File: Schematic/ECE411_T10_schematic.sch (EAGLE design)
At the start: 64 parts, among them IC1 LM386MM-1, J1 1, J2 DCJ0202, J3 AVR_SPI_PRG_6PTH, Q1 8.192 MHz, SW1 SPST_TACT-EVQQ2, U1 ATMEGA328P_PDIP

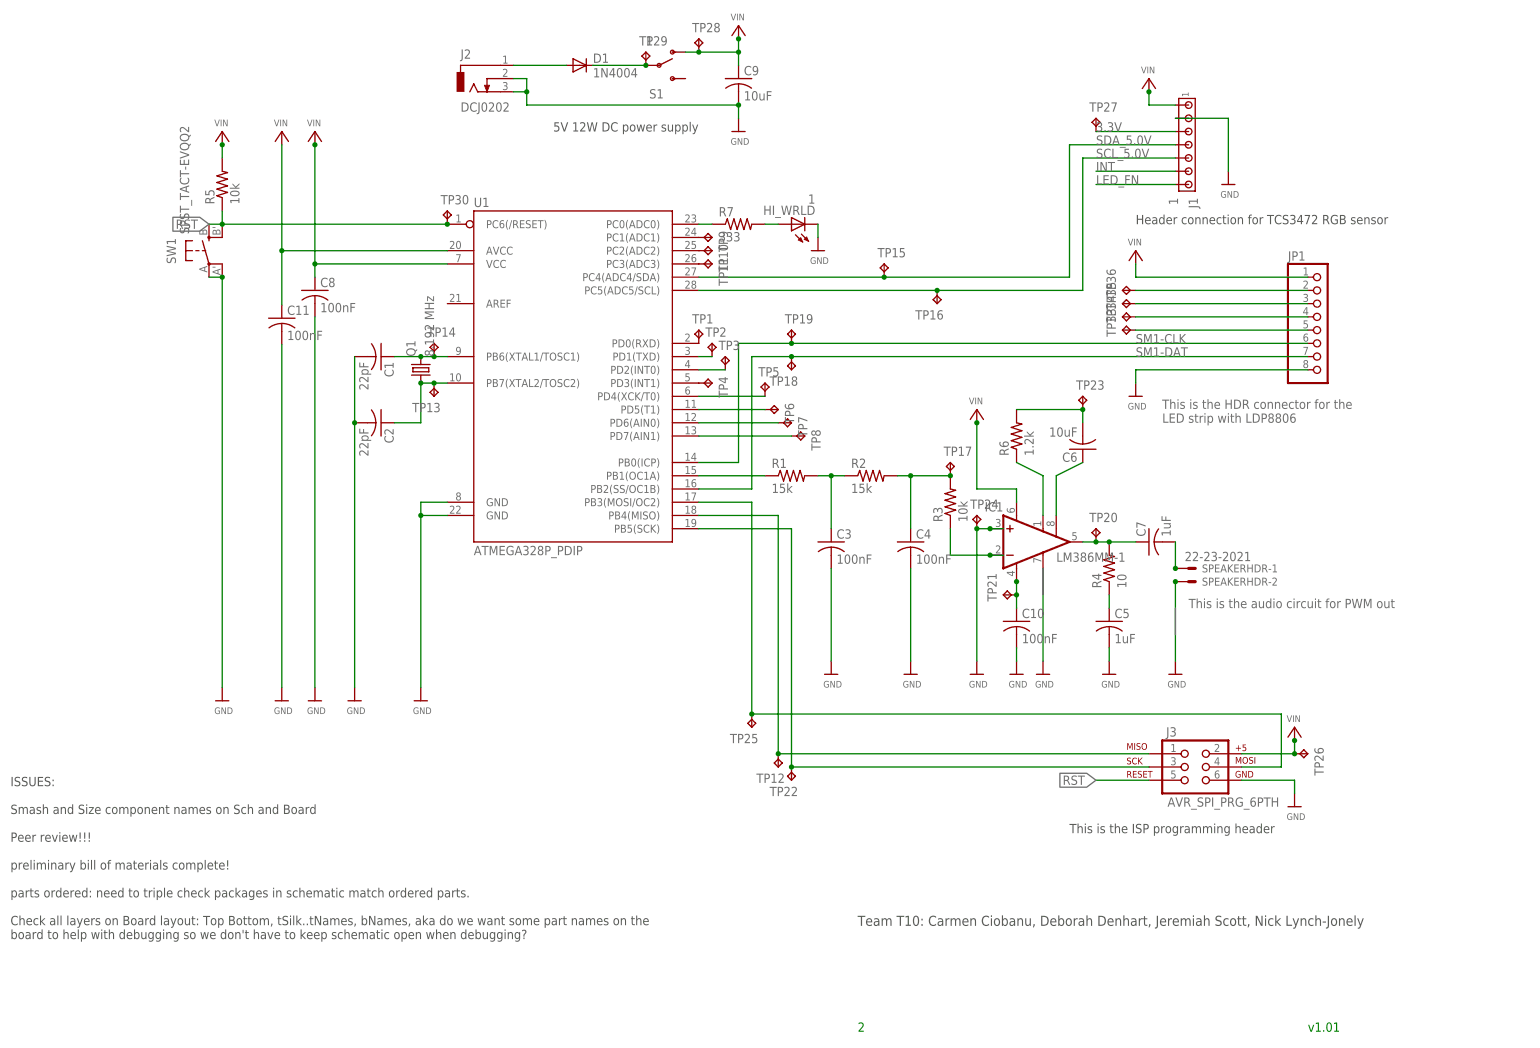
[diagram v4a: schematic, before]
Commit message: final layout candidate?
- fixed airwire @ (1.30, 1.05)
- smashed/sized some test points on Schematic
- updated dimension layer of board layout for better spacing of mounting
holes
- added team name info to both tPlace and tSilk layers
- png screenshots of final board layout candidate?
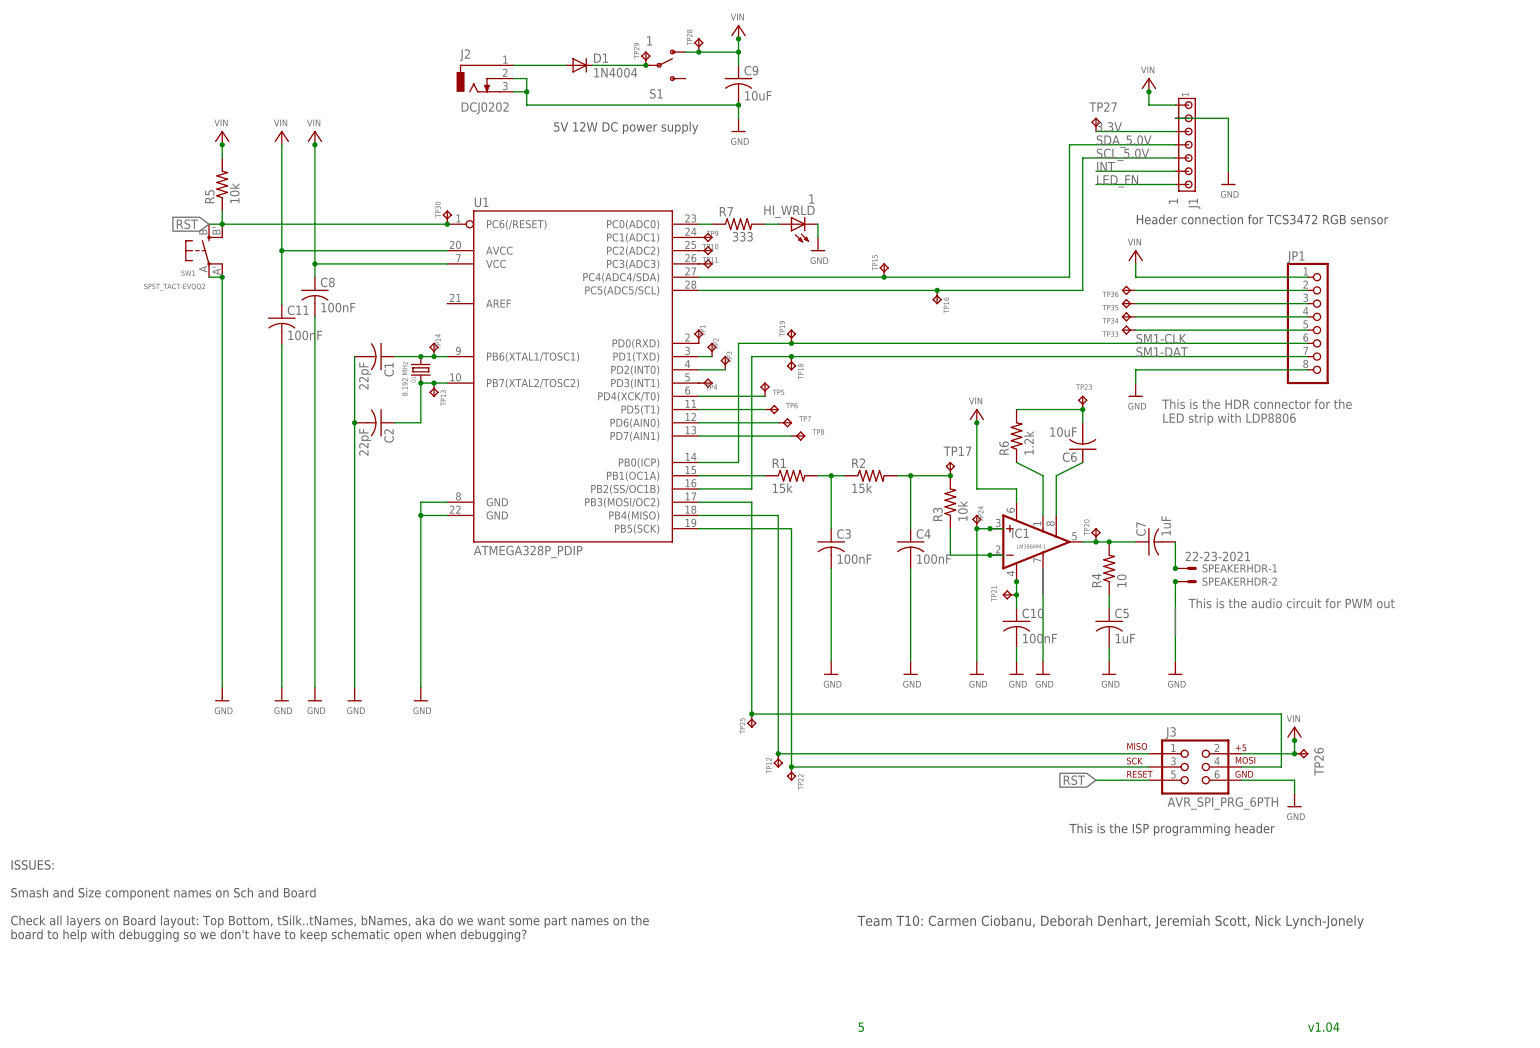
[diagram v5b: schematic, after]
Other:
- note added: "5"
- note added: "ISSUES: Smash and Size component names on Sch and Board Check all layers on Board layout: Top Bottom, tSilk..tNames, bNames, aka do we want some part names on the board to help with debugging so we don't have to keep schematic open when debugging?"
- note added: "v1.04"
- note removed: "2"
- note removed: "ISSUES: Smash and Size component names on Sch and Board Peer review!!! preliminary bill of materials complete! parts ordered: need to triple check packages in schematic match ordered parts. Check all layers on Board layout: Top Bottom, tSilk..tNames, bNames, aka do we want some part names on the board to help with debugging so we don't have to keep schematic open when debugging?"
- note removed: "v1.01"

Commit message: layout/schematic changes
- rerouted INT to PD2
- rerouted LED_FN to PC2
- increased trace size around pad connections
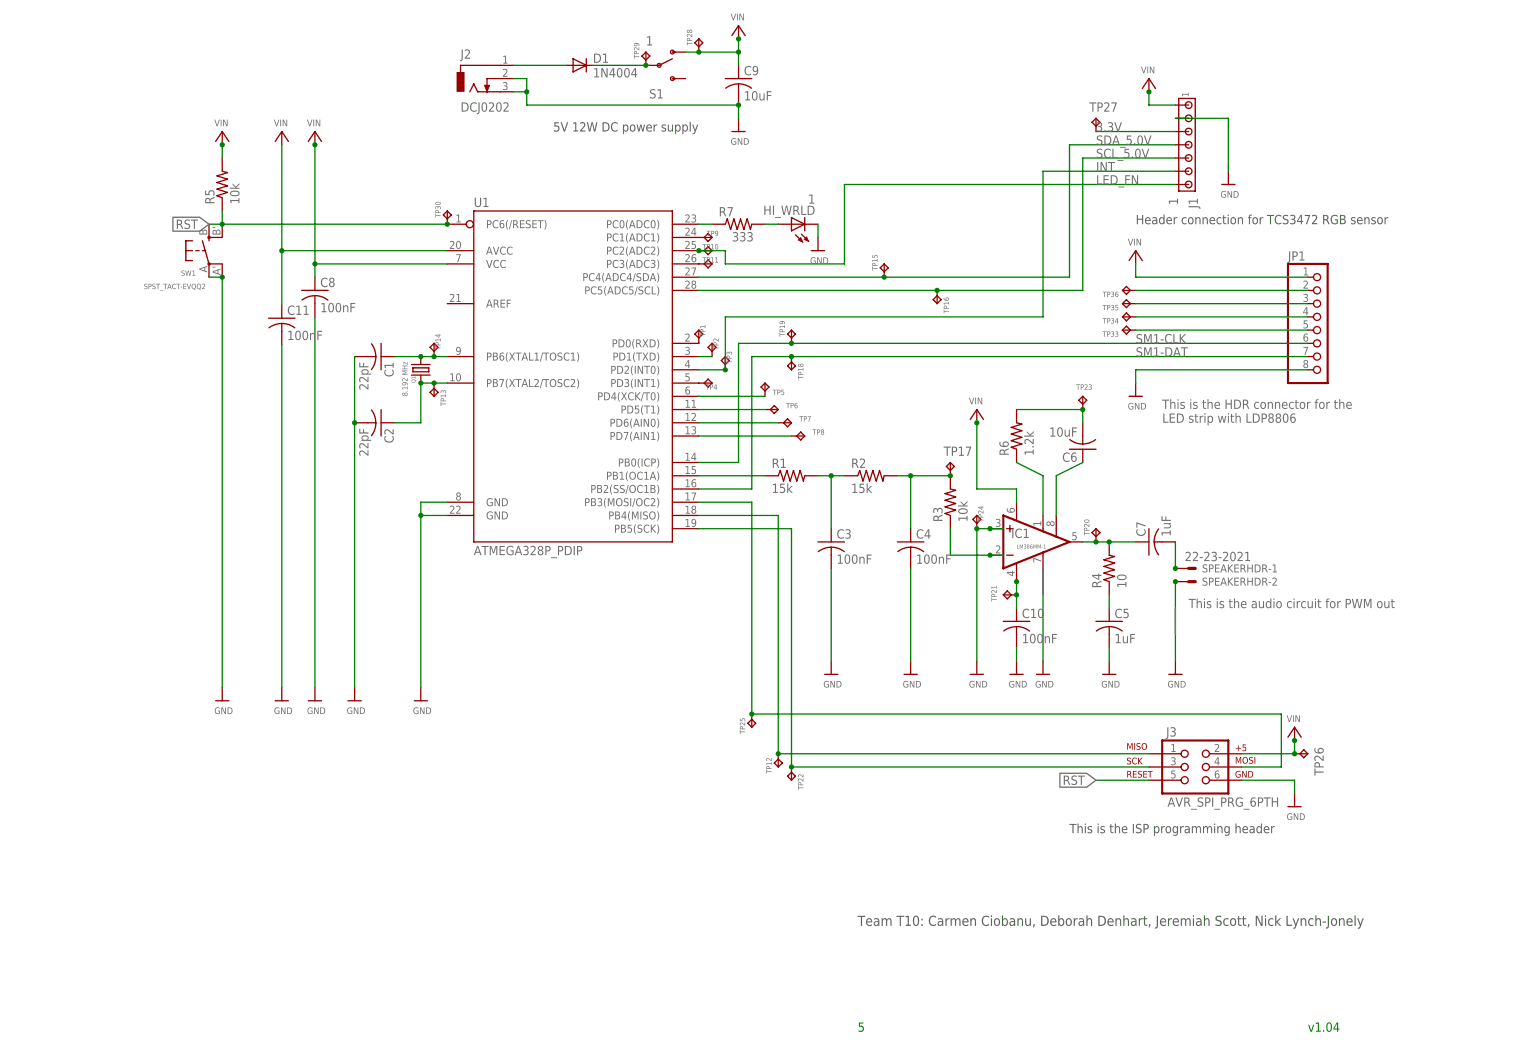
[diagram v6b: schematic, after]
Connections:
- removed net N$23: TP3.TP, U1.PD2(INT0)
- removed net N$29: TP10.TP, U1.PC2(ADC2)
- net INT: now also TP3.TP, U1.PD2(INT0)
- net LED_FN: now also TP10.TP, U1.PC2(ADC2)
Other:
- note removed: "ISSUES: Smash and Size component names on Sch and Board Check all layers on Board layout: Top Bottom, tSilk..tNames, bNames, aka do we want some part names on the board to help with debugging so we don't have to keep schematic open when debugging?"
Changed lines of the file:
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@@
 <text x="116.84" y="-106.68" size="1.778" layer="91">v1.04</text>
 <text x="30.48" y="-106.68" size="1.778" layer="91">5</text>
-<text x="-132.08" y="-88.9" size="1.778" layer="97">ISSUES:
-Smash and Size component names on Sch and Board
-Check all layers on Board layout: Top Bottom, tSilk..tNames, bNames, aka do we want some part names on the
-board to help with debugging so we don't have to keep schematic open when debugging?
-</text>
+<text x="-132.08" y="-88.9" size="1.778" layer="97"></text>
 <text x="71.12" y="-68.58" size="1.778" layer="97">This is the ISP programming header</text>
 </plain>
@@
 </segment>
 </net>
-<net name="N$23" class="0">
-<segment>
+<net name="N$24" class="0">
+<segment>
+<pinref part="U1" gate="G$1" pin="PD3(INT1)"/>
+<pinref part="TP4" gate="G$1" pin="TP"/>
+</segment>
+</net>
+<net name="N$25" class="0">
+<segment>
+<pinref part="U1" gate="G$1" pin="PD5(T1)"/>
+<pinref part="TP6" gate="G$1" pin="TP"/>
+<wire x1="12.7" y1="12.7" x2="0" y2="12.7" width="0.1524" layer="91"/>
+</segment>
+</net>
+<net name="N$26" class="0">
+<segment>
+<pinref part="U1" gate="G$1" pin="PD6(AIN0)"/>
+<pinref part="TP7" gate="G$1" pin="TP"/>
+<wire x1="0" y1="10.16" x2="15.24" y2="10.16" width="0.1524" layer="91"/>
+</segment>
+</net>
+<net name="N$27" class="0">
+<segment>
+<pinref part="U1" gate="G$1" pin="PD7(AIN1)"/>
+<pinref part="TP8" gate="G$1" pin="TP"/>
+<wire x1="0" y1="7.62" x2="17.78" y2="7.62" width="0.1524" layer="91"/>
+</segment>
+</net>
+<net name="N$28" class="0">
+<segment>
+<pinref part="U1" gate="G$1" pin="PC1(ADC1)"/>
+<pinref part="TP9" gate="G$1" pin="TP"/>
+</segment>
+</net>
+<net name="N$30" class="0">
+<segment>
+<pinref part="U1" gate="G$1" pin="PC3(ADC3)"/>
+<pinref part="TP11" gate="G$1" pin="TP"/>
+</segment>
+</net>
+<net name="INT" class="0">
+<segment>
+<pinref part="J1" gate="G$1" pin="6"/>
+<wire x1="91.44" y1="58.42" x2="66.04" y2="58.42" width="0.1524" layer="91"/>
+<label x="76.2" y="58.42" size="1.778" layer="95"/>
+<wire x1="66.04" y1="58.42" x2="66.04" y2="30.48" width="0.1524" layer="91"/>
+<wire x1="66.04" y1="30.48" x2="5.08" y2="30.48" width="0.1524" layer="91"/>
 <pinref part="U1" gate="G$1" pin="PD2(INT0)"/>
 <pinref part="TP3" gate="G$1" pin="TP"/>
 <wire x1="0" y1="20.32" x2="5.08" y2="20.32" width="0.1524" layer="91"/>
-</segment>
-</net>
-<net name="N$24" class="0">
-<segment>
-<pinref part="U1" gate="G$1" pin="PD3(INT1)"/>
-<pinref part="TP4" gate="G$1" pin="TP"/>
-</segment>
-</net>
-<net name="N$25" class="0">
-<segment>
-<pinref part="U1" gate="G$1" pin="PD5(T1)"/>
-<pinref part="TP6" gate="G$1" pin="TP"/>
-<wire x1="12.7" y1="12.7" x2="0" y2="12.7" width="0.1524" layer="91"/>
-</segment>
-</net>
-<net name="N$26" class="0">
-<segment>
-<pinref part="U1" gate="G$1" pin="PD6(AIN0)"/>
-<pinref part="TP7" gate="G$1" pin="TP"/>
-<wire x1="0" y1="10.16" x2="15.24" y2="10.16" width="0.1524" layer="91"/>
-</segment>
-</net>
-<net name="N$27" class="0">
-<segment>
-<pinref part="U1" gate="G$1" pin="PD7(AIN1)"/>
-<pinref part="TP8" gate="G$1" pin="TP"/>
-<wire x1="0" y1="7.62" x2="17.78" y2="7.62" width="0.1524" layer="91"/>
-</segment>
-</net>
-<net name="N$28" class="0">
-<segment>
-<pinref part="U1" gate="G$1" pin="PC1(ADC1)"/>
-<pinref part="TP9" gate="G$1" pin="TP"/>
-</segment>
-</net>
-<net name="N$29" class="0">
-<segment>
+<wire x1="5.08" y1="30.48" x2="5.08" y2="20.32" width="0.1524" layer="91"/>
+<junction x="5.08" y="20.32"/>
+</segment>
+</net>
+<net name="LED_FN" class="0">
+<segment>
+<pinref part="J1" gate="G$1" pin="7"/>
+<label x="76.2" y="55.88" size="1.778" layer="95"/>
+<wire x1="91.44" y1="55.88" x2="27.94" y2="55.88" width="0.1524" layer="91"/>
+<wire x1="27.94" y1="55.88" x2="27.94" y2="40.64" width="0.1524" layer="91"/>
+<wire x1="27.94" y1="40.64" x2="5.08" y2="40.64" width="0.1524" layer="91"/>
+<wire x1="5.08" y1="40.64" x2="5.08" y2="43.18" width="0.1524" layer="91"/>
 <pinref part="U1" gate="G$1" pin="PC2(ADC2)"/>
 <pinref part="TP10" gate="G$1" pin="TP"/>
-</segment>
-</net>
-<net name="N$30" class="0">
-<segment>
-<pinref part="U1" gate="G$1" pin="PC3(ADC3)"/>
-<pinref part="TP11" gate="G$1" pin="TP"/>
-</segment>
-</net>
-<net name="INT" class="0">
-<segment>
-<pinref part="J1" gate="G$1" pin="6"/>
-<wire x1="91.44" y1="58.42" x2="76.2" y2="58.42" width="0.1524" layer="91"/>
-<label x="76.2" y="58.42" size="1.778" layer="95"/>
-</segment>
-</net>
-<net name="LED_FN" class="0">
-<segment>
-<pinref part="J1" gate="G$1" pin="7"/>
-<wire x1="91.44" y1="55.88" x2="76.2" y2="55.88" width="0.1524" layer="91"/>
-<label x="76.2" y="55.88" size="1.778" layer="95"/>
-</segment>
-</net>
+<wire x1="5.08" y1="43.18" x2="0" y2="43.18" width="0.1524" layer="91"/>
+<junction x="0" y="43.18"/>
+</segment>
+</net>
